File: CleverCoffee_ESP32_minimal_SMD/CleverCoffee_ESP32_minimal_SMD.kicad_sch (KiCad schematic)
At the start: 25 parts

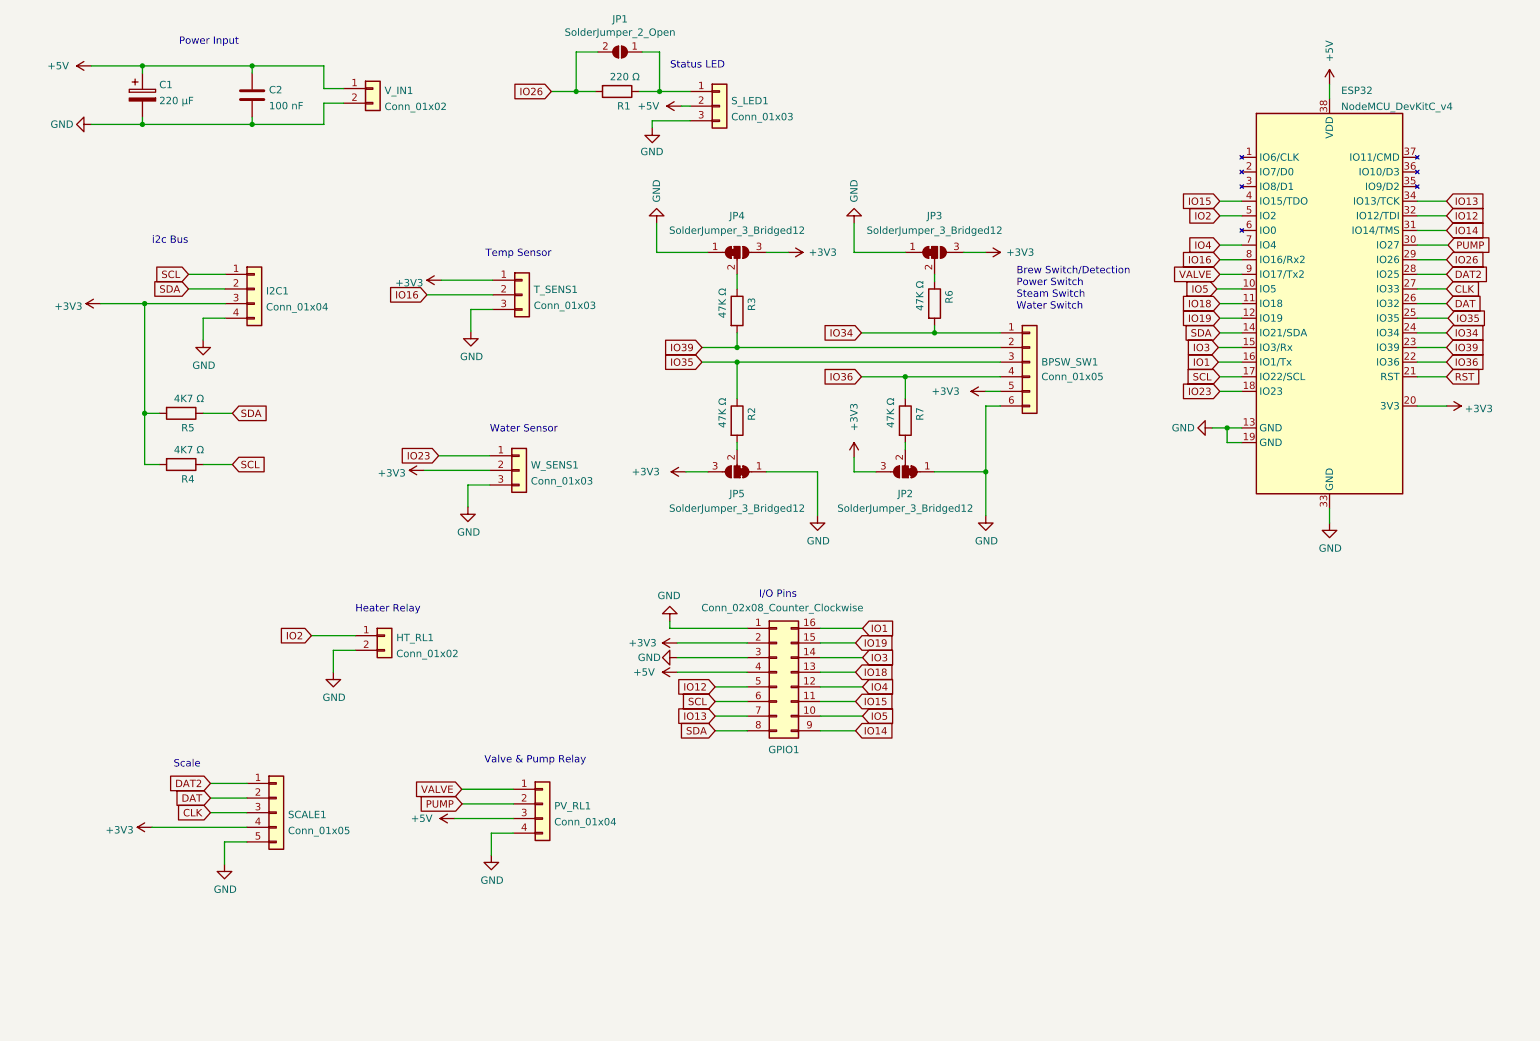
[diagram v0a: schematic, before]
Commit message: draft enc header + dallas
added enc header, lables for enc and buttons
reduce gpio1 to 2x7, because 3 IO moved to enc header
added inline resistor und parallel cap for tsic
added solder joined pull up for dallas temp sensor
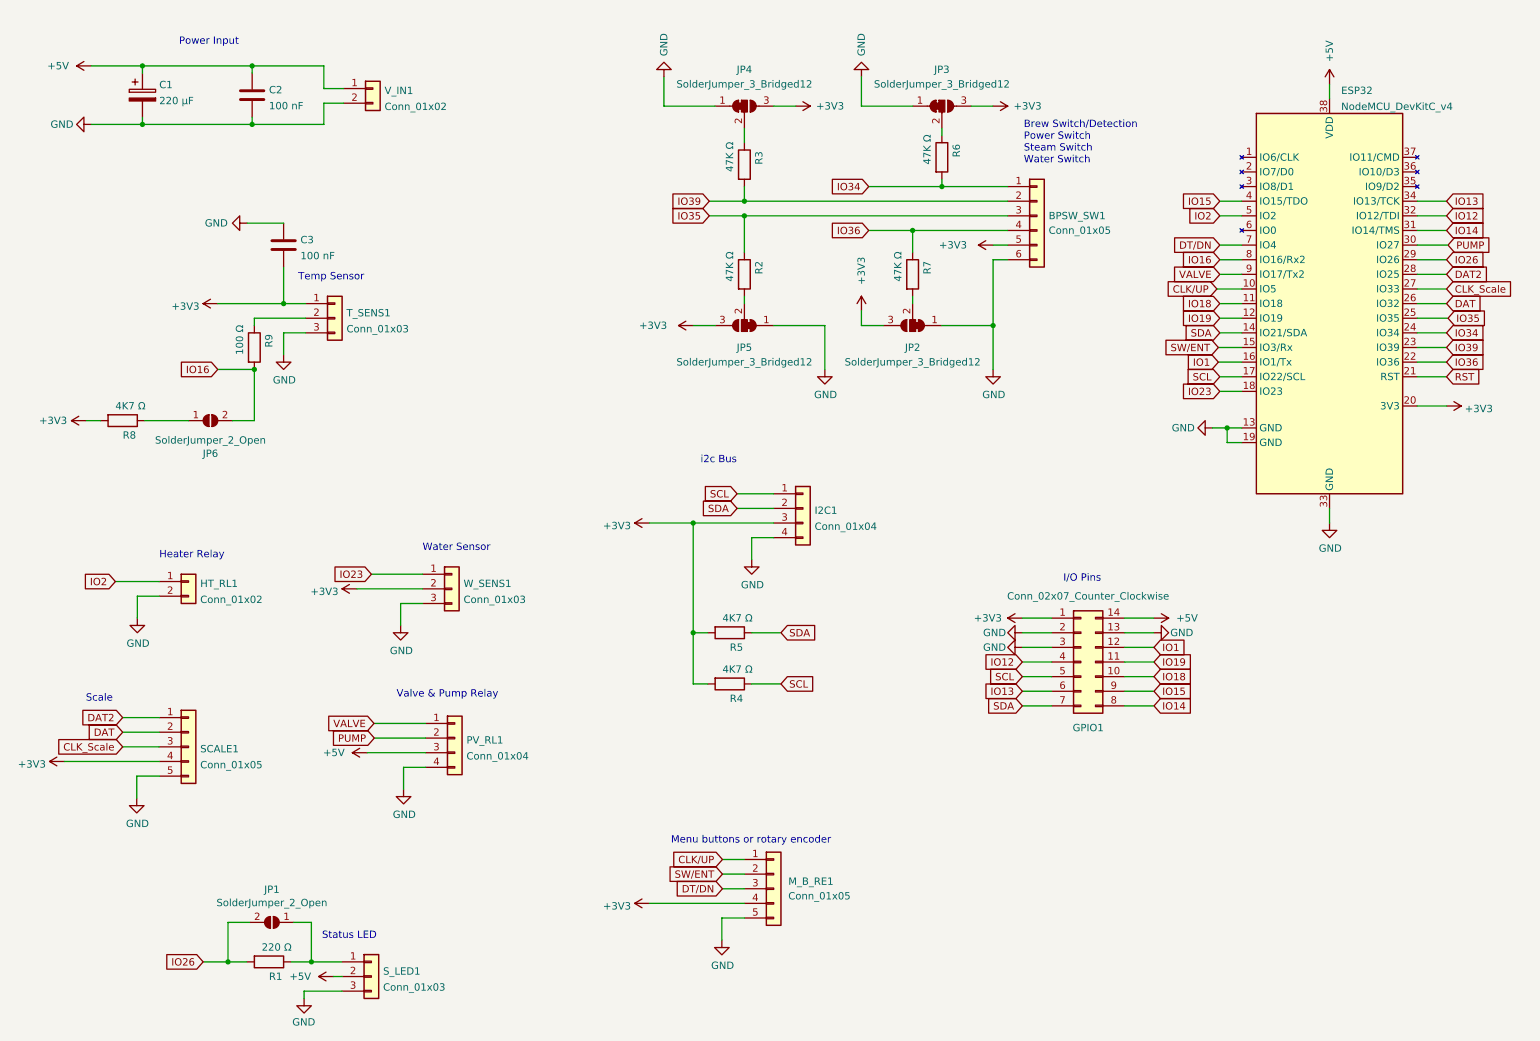
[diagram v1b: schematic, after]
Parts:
- removed GPIO1: Conn_02x08_Counter_Clockwise, Connector_PinSocket_2.54mm:PinSocket_2x08_P2.54mm_Vertical, symbol Connector_Generic:Conn_02x08_Counter_Clockwise
- added C3: 100 nF, Capacitor_SMD:C_1206_3216Metric_Pad1.33x1.80mm_HandSolder, symbol Device:C
- added GPIO1: Conn_02x07_Counter_Clockwise, Connector_PinSocket_2.54mm:PinSocket_2x07_P2.54mm_Vertical, symbol Connector_Generic:Conn_02x07_Counter_Clockwise
- added JP6: SolderJumper_2_Open, Jumper:SolderJumper-2_P1.3mm_Open_Pad1.0x1.5mm, symbol Jumper:SolderJumper_2_Open
- added M_B_RE1: Conn_01x05, Connector_PinSocket_2.54mm:PinSocket_1x05_P2.54mm_Vertical, symbol Connector_Generic:Conn_01x05
- added R8: 4K7 Ω, Resistor_SMD:R_1206_3216Metric_Pad1.30x1.75mm_HandSolder, symbol Device:R
- added R9: 100 Ω, Resistor_SMD:R_1206_3216Metric_Pad1.30x1.75mm_HandSolder, symbol Device:R
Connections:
- net +3V3: now also C3.2, GPIO1.1 (Pin_1), M_B_RE1.4 (Pin_4), R8.2
- net +5V: now also GPIO1.14 (Pin_14)
- net GND: now also C3.1, GPIO1.13 (Pin_13), GPIO1.2 (Pin_2), GPIO1.3 (Pin_3), M_B_RE1.5 (Pin_5)
- net IO1: now also GPIO1.12 (Pin_12)
- net IO12: now also GPIO1.4 (Pin_4)
- net IO13: now also GPIO1.6 (Pin_6)
- net IO14: now also GPIO1.8 (Pin_8)
- net IO15: now also GPIO1.9 (Pin_9)
- net IO16: now also JP6.2 (B), R9.2; no longer T_SENS1.2 (Pin_2)
- net IO18: now also GPIO1.10 (Pin_10)
- net IO19: now also GPIO1.11 (Pin_11)
- net SCL: now also GPIO1.5 (Pin_5)
- net SDA: now also GPIO1.7 (Pin_7)
- net CLK renamed CLK_Scale
- net IO3 renamed SW/ENT
- net IO4 renamed DT/DN
- net IO5 renamed CLK/UP
- new net: JP6.1 (A), R8.1
- new net: R9.1, T_SENS1.2 (Pin_2)
- new net CLK/UP: M_B_RE1.1 (Pin_1)
- new net DT/DN: M_B_RE1.3 (Pin_3)
- new net SW/ENT: M_B_RE1.2 (Pin_2)
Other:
- note added: "Menu buttons or rotary encoder"
- moved on the sheet: BPSW_SW1, HT_RL1, I2C1, JP1, JP2, JP3, JP4, JP5, PV_RL1, R1, R2, R3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

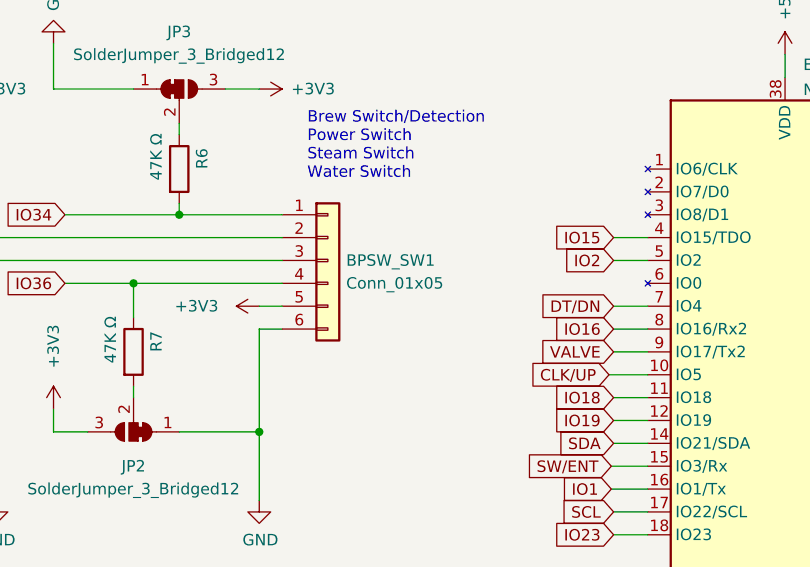
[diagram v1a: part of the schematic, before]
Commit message: change terminal footprints to jst xh
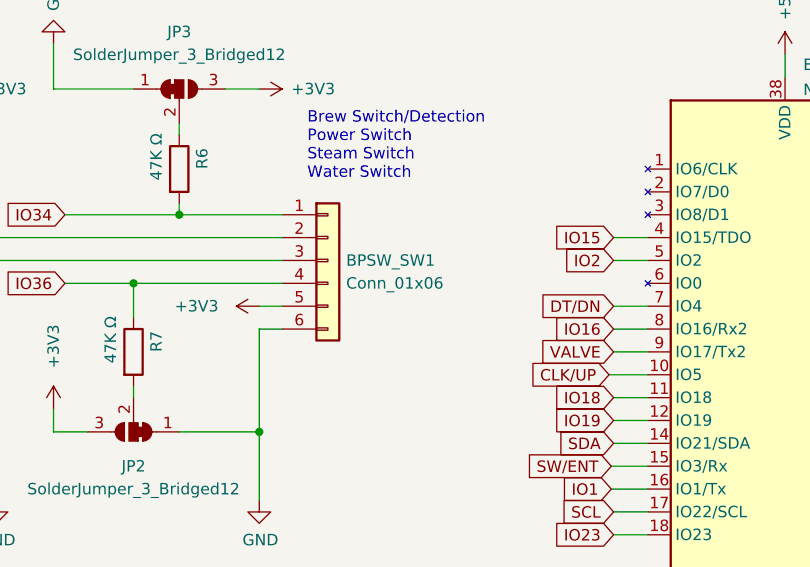
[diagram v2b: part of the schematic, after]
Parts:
- BPSW_SW1: value Conn_01x05 -> Conn_01x06; footprint Connector_PinSocket_2.54mm:PinSocket_1x06_P2.54mm_Vertical -> Connector_JST:JST_XH_S6B-XH-A-1_1x06_P2.50mm_Horizontal
- HT_RL1, V_IN1: footprint Connector_PinSocket_2.54mm:PinSocket_1x02_P2.54mm_Vertical -> Connector_JST:JST_XH_S2B-XH-A-1_1x02_P2.50mm_Horizontal
- I2C1, PV_RL1: footprint Connector_PinSocket_2.54mm:PinSocket_1x04_P2.54mm_Vertical -> Connector_JST:JST_XH_S4B-XH-A-1_1x04_P2.50mm_Horizontal
- M_B_RE1, SCALE1: footprint Connector_PinSocket_2.54mm:PinSocket_1x05_P2.54mm_Vertical -> Connector_JST:JST_XH_S5B-XH-A-1_1x05_P2.50mm_Horizontal
- S_LED1, T_SENS1, W_SENS1: footprint Connector_PinSocket_2.54mm:PinSocket_1x03_P2.54mm_Vertical -> Connector_JST:JST_XH_S3B-XH-A-1_1x03_P2.50mm_Horizontal
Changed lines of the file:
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@@
 			)
 		)
-		(property "Footprint" "Connector_PinSocket_2.54mm:PinSocket_1x02_P2.54mm_Vertical"
+		(property "Footprint" "Connector_JST:JST_XH_S2B-XH-A-1_1x02_P2.50mm_Horizontal"
 			(at 48.26 114.3 0)
 			(hide yes)
@@
 			)
 		)
-		(property "Footprint" "Connector_PinSocket_2.54mm:PinSocket_1x03_P2.54mm_Vertical"
+		(property "Footprint" "Connector_JST:JST_XH_S3B-XH-A-1_1x03_P2.50mm_Horizontal"
 			(at 93.98 115.57 0)
 			(hide yes)
@@
 			)
 		)
-		(property "Value" "Conn_01x05"
+		(property "Value" "Conn_01x06"
 			(at 197.612 53.34 0)
 			(show_name no)
@@
 			)
 		)
-		(property "Footprint" "Connector_PinSocket_2.54mm:PinSocket_1x06_P2.54mm_Vertical"
+		(property "Footprint" "Connector_JST:JST_XH_S6B-XH-A-1_1x06_P2.50mm_Horizontal"
 			(at 195.58 50.8 0)
 			(hide yes)
@@
 			)
 		)
-		(property "Footprint" "Connector_PinSocket_2.54mm:PinSocket_1x02_P2.54mm_Vertical"
+		(property "Footprint" "Connector_JST:JST_XH_S2B-XH-A-1_1x02_P2.50mm_Horizontal"
 			(at 80.264 28.702 0)
 			(hide yes)
@@
 			)
 		)
-		(property "Footprint" "Connector_PinSocket_2.54mm:PinSocket_1x05_P2.54mm_Vertical"
+		(property "Footprint" "Connector_JST:JST_XH_S5B-XH-A-1_1x05_P2.50mm_Horizontal"
 			(at 48.26 143.002 0)
 			(hide yes)
@@
 			)
 		)
-		(property "Footprint" "Connector_PinSocket_2.54mm:PinSocket_1x03_P2.54mm_Vertical"
+		(property "Footprint" "Connector_JST:JST_XH_S3B-XH-A-1_1x03_P2.50mm_Horizontal"
 			(at 80.01 182.88 0)
 			(hide yes)
@@
 			)
 		)
-		(property "Footprint" "Connector_PinSocket_2.54mm:PinSocket_1x05_P2.54mm_Vertical"
+		(property "Footprint" "Connector_JST:JST_XH_S5B-XH-A-1_1x05_P2.50mm_Horizontal"
 			(at 149.86 167.64 0)
 			(hide yes)
@@
 			)
 		)
-		(property "Footprint" "Connector_PinSocket_2.54mm:PinSocket_1x04_P2.54mm_Vertical"
+		(property "Footprint" "Connector_JST:JST_XH_S4B-XH-A-1_1x04_P2.50mm_Horizontal"
 			(at 154.94 101.6 0)
 			(hide yes)
@@
 			)
 		)
-		(property "Footprint" "Connector_PinSocket_2.54mm:PinSocket_1x04_P2.54mm_Vertical"
+		(property "Footprint" "Connector_JST:JST_XH_S4B-XH-A-1_1x04_P2.50mm_Horizontal"
 			(at 94.488 141.478 0)
 			(hide yes)
@@
 			)
 		)
-		(property "Footprint" "Connector_PinSocket_2.54mm:PinSocket_1x03_P2.54mm_Vertical"
+		(property "Footprint" "Connector_JST:JST_XH_S3B-XH-A-1_1x03_P2.50mm_Horizontal"
 			(at 73.66 68.58 0)
 			(hide yes)

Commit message: draft pcb layout
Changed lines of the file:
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@@
 	(wire
 		(pts
-			(xy 226.822 63.5) (xy 231.14 63.5)
-		)
-		(stroke
-			(width 0)
-			(type default)
-		)
-	)
-	(wire
-		(pts
 			(xy 227.33 68.58) (xy 231.14 68.58)
 		)
@@
 	(wire
 		(pts
+			(xy 227.33 63.5) (xy 231.14 63.5)
+		)
+		(stroke
+			(width 0)
+			(type default)
+		)
+	)
+	(wire
+		(pts
 			(xy 261.62 76.2) (xy 266.7 76.2)
 		)
@@
 	(global_label "CLK/UP"
 		(shape input)
-		(at 226.822 63.5 180)
+		(at 227.33 63.5 180)
 		(fields_autoplaced yes)
 		(effects
@@
 		)
 		(property "Intersheetrefs" "${INTERSHEET_REFS}"
-			(at 221.2641 63.4206 0)
+			(at 221.7721 63.4206 0)
 			(hide yes)
 			(show_name no)
@@
 	)
 	(symbol
+		(lib_name "+3.3V_1")
 		(lib_id "power:+3.3V")
 		(at 266.7 83.82 270)
@@
 			)
 		)
-		(property "Description" ""
+		(property "Description" "Power symbol creates a global label with name \"+3.3V\""
 			(at 266.7 83.82 0)
 			(hide yes)
